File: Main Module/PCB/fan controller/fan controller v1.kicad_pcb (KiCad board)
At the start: 2 copper layers, 37.2 x 22 mm, 38 parts, among them P1 AUX, P2 +12V Suppply, P3 FAN, Q1 NPN, U1 Octocoupler

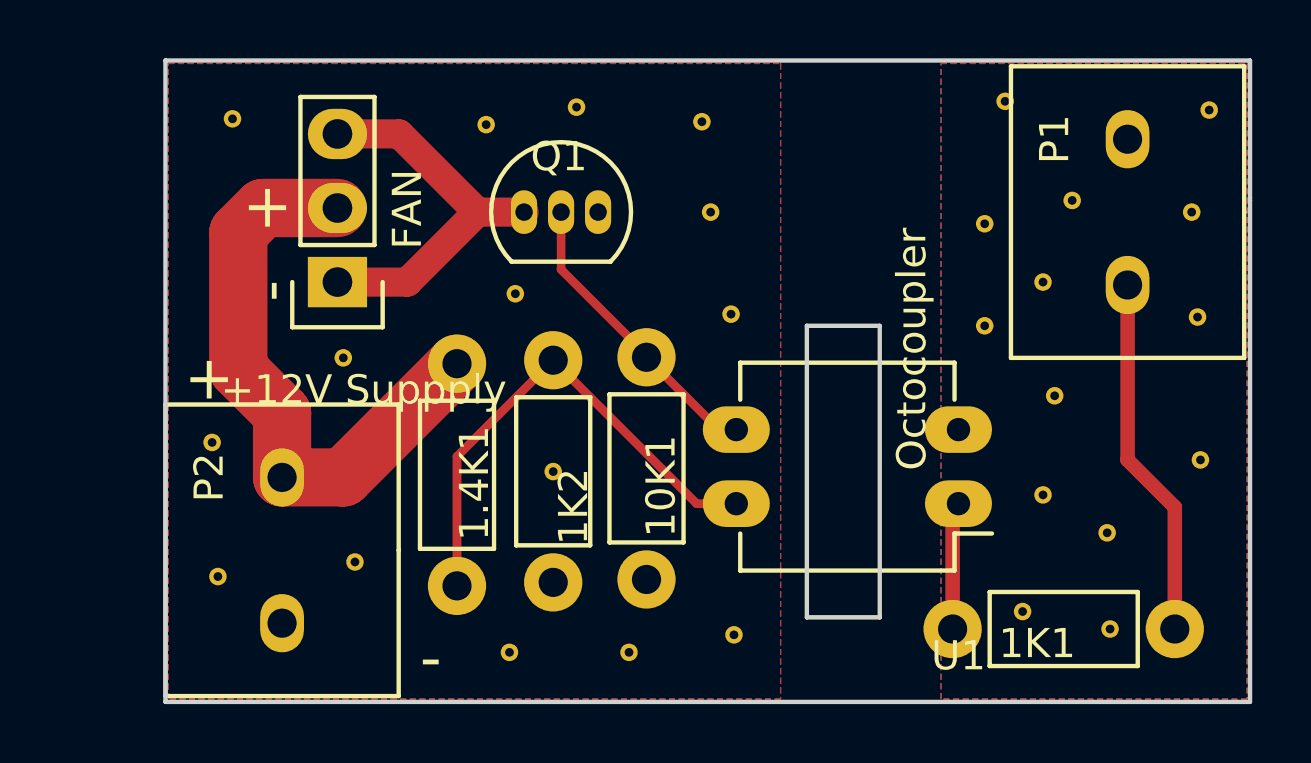
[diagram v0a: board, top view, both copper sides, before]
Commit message: * added solder pads for another fan header to the PCB. there is room ... might as well
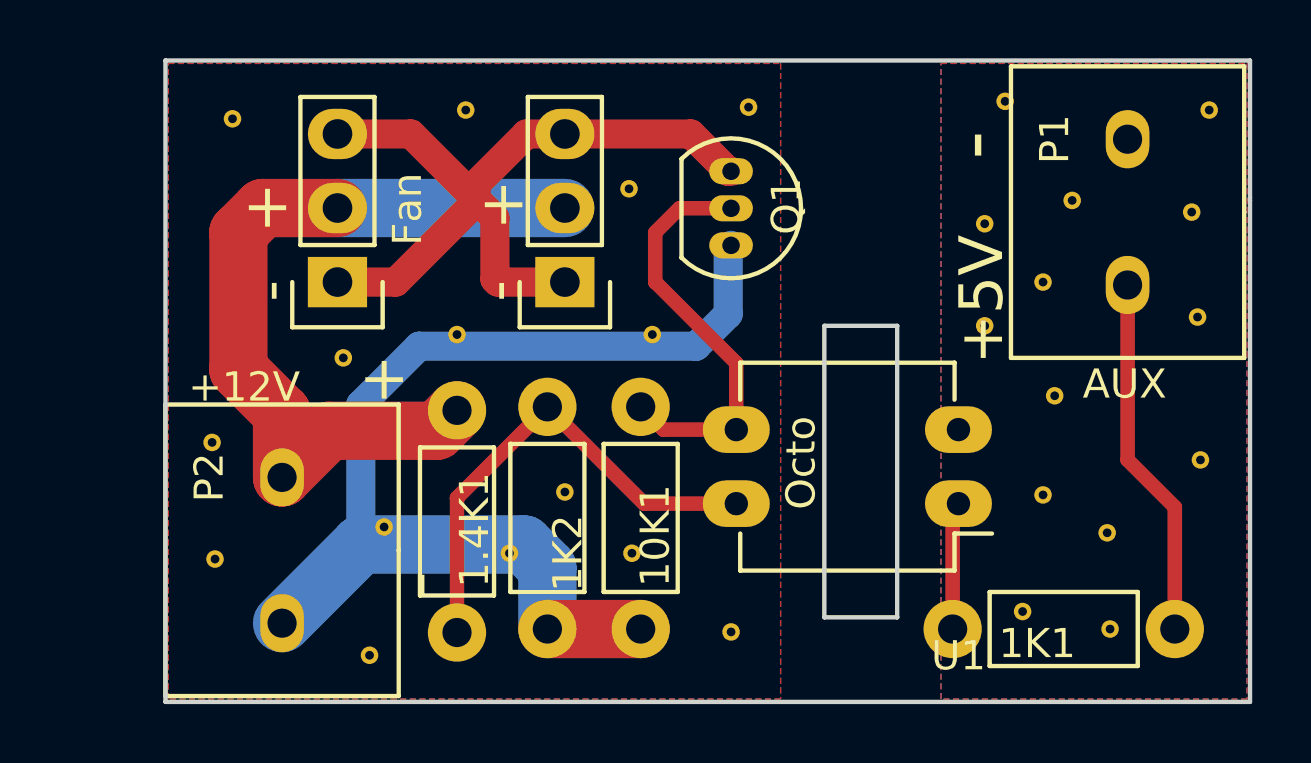
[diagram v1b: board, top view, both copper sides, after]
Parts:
- added P4: Fan, Pin_Headers:Pin_Header_Straight_1x03, F.Cu at (201.4, 128.5)
- P2: value +12V Suppply -> +12V
- P3: value FAN -> Fan
- U1: value Octocoupler -> Octo
- moved ? 15.5 mm to (203.7, 137.8)
- moved ? 8.81 mm to (197.7, 130.3)
- moved ? 8.19 mm to (199.5, 137.8)
- moved ? 7.59 mm to (201.4, 135.7)
- moved Q1 7.24 mm to (207.1, 124.7), turned to 270 degrees
- moved ? 6.53 mm to (198.0, 122.6)
- moved ? 6.10 mm to (195.2, 136.9)
- moved ? 4.80 mm to (194.7, 141.3)
- moved ? 3.57 mm to (207.1, 140.5)
- moved ? 2.91 mm to (203.6, 125.3)
- moved ? 2.79 mm to (204.4, 130.3)
- moved 10K1 1.71 mm to (204.0, 140.4)
- moved ? 1.68 mm to (207.7, 122.5)
- moved 1K2 1.61 mm to (200.8, 140.4)
- moved 1.4K1 1.60 mm to (197.7, 132.9)
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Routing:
- net GND: track 0.00 -> 36.9 mm
- net Net-(P3-Pad1): track 13.4 -> 27.7 mm
- net +12V: track 20.4 -> 27.6 mm
- net Net-(10K1-Pad2): track 10.3 -> 15.1 mm
- net Net-(1.4K1-Pad2): track 17.4 -> 16.9 mm
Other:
- outline, holes or cut-outs redrawn
- net class Default: clearance 0.23 -> 0.3; trace_width 0.3 -> 0.5
- rule trace_clearance: 0.23 -> 0.3
- rule trace_min: 0.23 -> 0.3
- board text added: "+5V"

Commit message: * corrected molex connectors on Fan PCB * added optional LED to show "ON" state
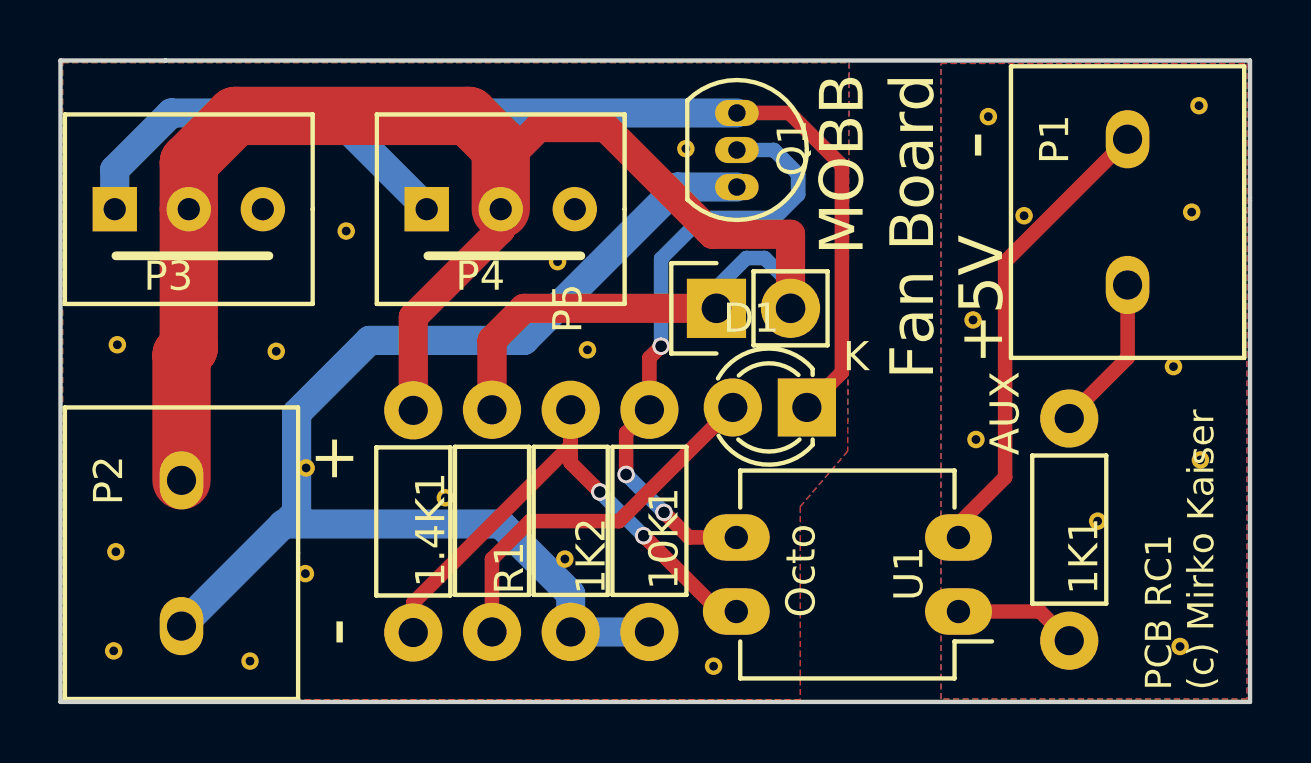
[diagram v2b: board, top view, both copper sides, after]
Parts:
- removed the ? at (189.3, 134.0)
- removed the ? at (203.7, 137.8)
- removed the ? at (203.6, 125.3)
- removed the ? at (218.8, 125.7)
- removed the ? at (220.0, 137.1)
- removed the ? at (218.2, 132.4)
- added ?: , MOBB-KiCad-Lib:VIA-0.6MM, F.Cu at (205.6, 123.9)
- added ?: , MOBB-KiCad-Lib:VIA-0.6MM, F.Cu at (192.5, 134.9)
- added ?: , MOBB-KiCad-Lib:VIA-0.6MM, F.Cu at (201.2, 127.8)
- added D1: LED, LEDs:LED-3MM, F.Cu at (209.7, 132.8)
- added P5: Jumper, Pin_Headers:Pin_Header_Straight_1x02, F.Cu at (206.6, 129.4)
- added R1: 1.5K, Resistors_ThroughHole:Resistor_Horizontal_RM7mm, F.Cu at (198.9, 140.5)
- P2: value +12V -> +12V Suppply
- P3, P4: footprint Pin_Headers:Pin_Header_Straight_1x03 -> MOBB-KiCad-Lib:Molex-KK-1x3P
- moved ? 21.4 mm to (185.9, 141.2)
- moved ? 14.4 mm to (186.1, 130.7)
- moved ? 14.4 mm to (206.5, 141.7)
- moved ? 9.99 mm to (202.2, 130.8)
- moved ? 9.64 mm to (190.6, 141.5)
- moved P3 5.68 mm to (188.5, 126.0)
- moved ? 5.48 mm to (193.9, 126.8)
- moved ? 4.03 mm to (219.7, 136.7)
- moved 1K1 4.02 mm to (218.7, 140.8), turned to 90 degrees
- moved U1 3.70 mm to (214.9, 139.8)
- moved ? 3.56 mm to (192.5, 138.5)
- moved P2 3.45 mm to (188.2, 137.8)
- moved ? 3.41 mm to (186.0, 137.8)
- moved P4 3.33 mm to (199.2, 126.0)
- moved ? 3.29 mm to (205.8, 143.5)
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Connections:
- P3 pad 1: Net-(P3-Pad1) -> Net-(D1-Pad1)
- P3 pad 3: Net-(P3-Pad1) -> Net-(P3-Pad3)
- P4 pad 1: Net-(P3-Pad1) -> Net-(D1-Pad1)
- P4 pad 3: Net-(P3-Pad1) -> Net-(P4-Pad3)
- Q1 pad 1: Net-(P3-Pad1) -> Net-(D1-Pad1)
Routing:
- net Net-(D1-Pad1): track 0.00 -> 41.3 mm
- net +12V: track 27.6 -> 64.5 mm
- net Net-(P3-Pad1): track 27.7 -> 0.00 mm
- net GNDA: track 0.00 -> 16.1 mm
- net Net-(D1-Pad2): track 0.00 -> 12.9 mm
- net +5V: track 12.5 -> 5.41 mm
- net Net-(10K1-Pad2): track 15.1 -> 21.3 mm, vias 0 -> 3
- net GND: track 36.9 -> 42.1 mm
- net Net-(1.4K1-Pad2): track 16.9 -> 20.0 mm, vias 0 -> 2
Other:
- board size 37.2 x 22 mm -> 40.8 x 22 mm
- board text added: "Cut"
- board text added: "MOBB Fan Board"
- board text added: "MOBB Fan Board (c) Mirko Kaiser"
- board text added: "PCB RC1 (c) Mirko Kaiser"
- board text added: "github.com/KaiserSoft/OpenSimButtonBox"

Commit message: * minor trace tweak
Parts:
- removed the ? at (223.2, 134.6)
- moved ? 1.89 mm to (190.7, 135.4)
- moved ? 1.61 mm to (221.2, 136.3)
- moved ? 0.80 mm to (193.3, 138.5)
- moved ? 0.74 mm to (197.6, 135.2)
- moved ? 0.69 mm to (202.0, 137.7)
- moved P5 0.55 mm to (206.6, 128.8)
- moved ? 0.41 mm to (216.8, 126.0)
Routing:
- net Net-(10K1-Pad2): track 21.3 -> 24.7 mm, vias 3 -> 2
- net +12V: track 64.5 -> 66.1 mm

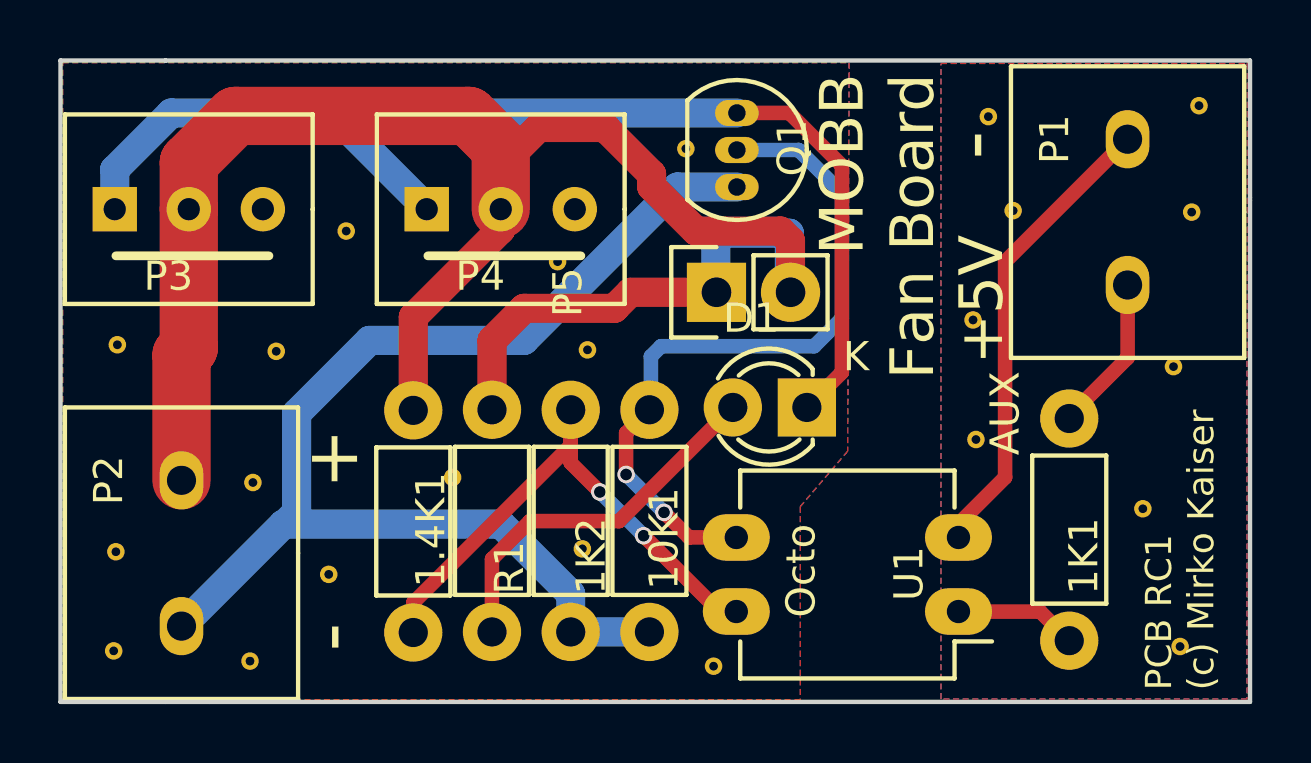
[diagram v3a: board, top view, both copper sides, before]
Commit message: * RC1 final for fan controller * ordered V-CUT version today since that fits into 5*5cm order size
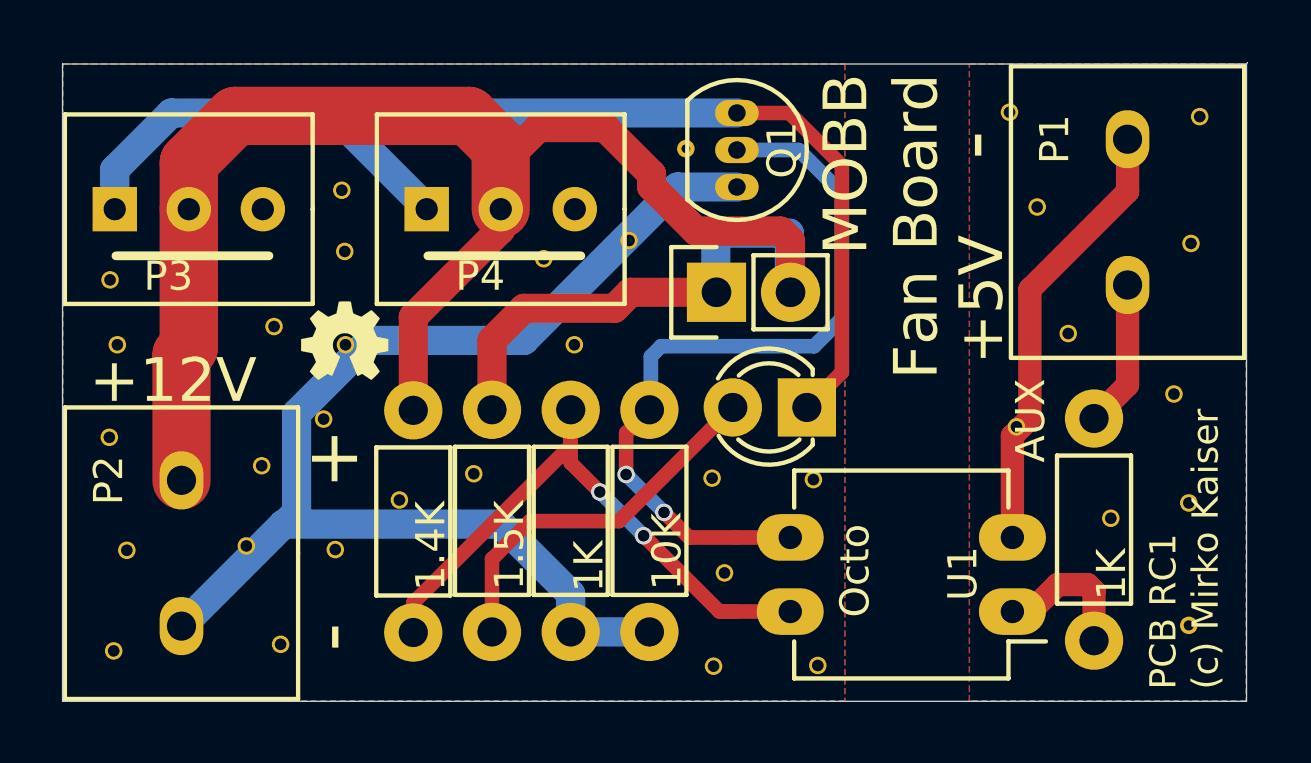
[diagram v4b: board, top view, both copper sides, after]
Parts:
- removed the ? at (215.4, 129.8)
- removed the ? at (202.0, 137.7)
- removed the ? at (202.2, 130.8)
- removed the ? at (215.5, 133.9)
- added ?: , MOBB-KiCad-Lib:VIA-0.6MM, F.Cu at (216.9, 133.5)
- added ?: , MOBB-KiCad-Lib:VIA-0.6MM, F.Cu at (195.7, 136.0)
- added ?: , MOBB-KiCad-Lib:VIA-0.6MM, F.Cu at (193.1, 133.2)
- added ?: , MOBB-KiCad-Lib:VIA-0.6MM, F.Cu at (201.7, 130.7)
- added ?: , MOBB-KiCad-Lib:VIA-0.6MM, F.Cu at (203.6, 127.1)
- added ?: , MOBB-KiCad-Lib:VIA-0.6MM, F.Cu at (185.8, 128.4)
- added ?: , MOBB-KiCad-Lib:VIA-0.6MM, F.Cu at (193.8, 127.5)
- added ?: , MOBB-KiCad-Lib:VIA-0.6MM, F.Cu at (191.4, 130.0)
- added ?: , MOBB-KiCad-Lib:VIA-0.6MM, F.Cu at (220.1, 136.6)
- added ?: , MOBB-KiCad-Lib:VIA-0.6MM, F.Cu at (218.7, 130.3)
- added ?: , MOBB-KiCad-Lib:VIA-0.6MM, F.Cu at (185.8, 133.8)
- added ?: , MOBB-KiCad-Lib:VIA-0.6MM, F.Cu at (209.9, 135.3)
- added ?: , MOBB-KiCad-Lib:VIA-0.6MM, F.Cu at (206.9, 138.5)
- added ?: , MOBB-KiCad-Lib:VIA-0.6MM, F.Cu at (206.4, 135.2)
- added ?: , MOBB-KiCad-Lib:VIA-0.6MM, F.Cu at (210.1, 141.7)
- added ?: , MOBB-KiCad-Lib:VIA-0.6MM, F.Cu at (190.5, 137.6)
- added G***: LOGO, MOBB-KiCad-Lib:OPEN_HW_LOGO_3MM, F.Cu at (193.8, 130.5)
- added G***: LOGO, MOBB-KiCad-Lib:OPEN_HW_LOGO_3MM, B.Cu at (213.1, 134.1)
- 1.5K: renamed from R1; value 1.5K -> R
- moved ? 2.39 mm to (193.9, 130.7)
- moved ? 2.28 mm to (205.7, 141.2)
- moved U1 1.85 mm to (216.8, 139.8)
- moved ? 1.59 mm to (222.8, 136.1)
- moved ? 1.41 mm to (193.8, 125.3)
- moved ? 1.20 mm to (191.7, 140.9)
- moved ? 1.08 mm to (222.9, 127.2)
- moved ? 0.94 mm to (222.3, 132.3)
- moved ? 0.88 mm to (193.5, 137.7)
- moved 1K 0.85 mm to (219.6, 140.8)
- moved ? 0.83 mm to (217.6, 125.9)
- moved ? 0.78 mm to (222.8, 140.3)
- moved ? 0.74 mm to (216.7, 122.7)
- moved ? 0.74 mm to (198.3, 135.1)
- moved ? 0.65 mm to (191.0, 134.8)
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- renumbered 1.4K1 to 1.4K, 10K1 to 10K, 1K1 to 1K, 1K2 to 1K
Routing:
- net Net-(10K1-Pad2): track 24.7 -> 26.5 mm
- net Net-(1.4K1-Pad2): track 20.0 -> 21.8 mm
- net GNDA: track 16.1 -> 15.3 mm
- net Net-(1K1-Pad1): track 4.21 -> 4.98 mm
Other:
- board size 40.8 x 22 mm -> 40.6 x 21.9 mm
- net class 5V: trace_width 0.5 -> 0.8
- board text added: "+12V"
- board text added: "MOBB Fan Board (c) 2016 Mirko Kaiser"
- board text removed: "MOBB Fan Board (c) Mirko Kaiser"
